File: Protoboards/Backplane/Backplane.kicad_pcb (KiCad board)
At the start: 2 copper layers, 129.5 x 142.2 mm, 2501 parts

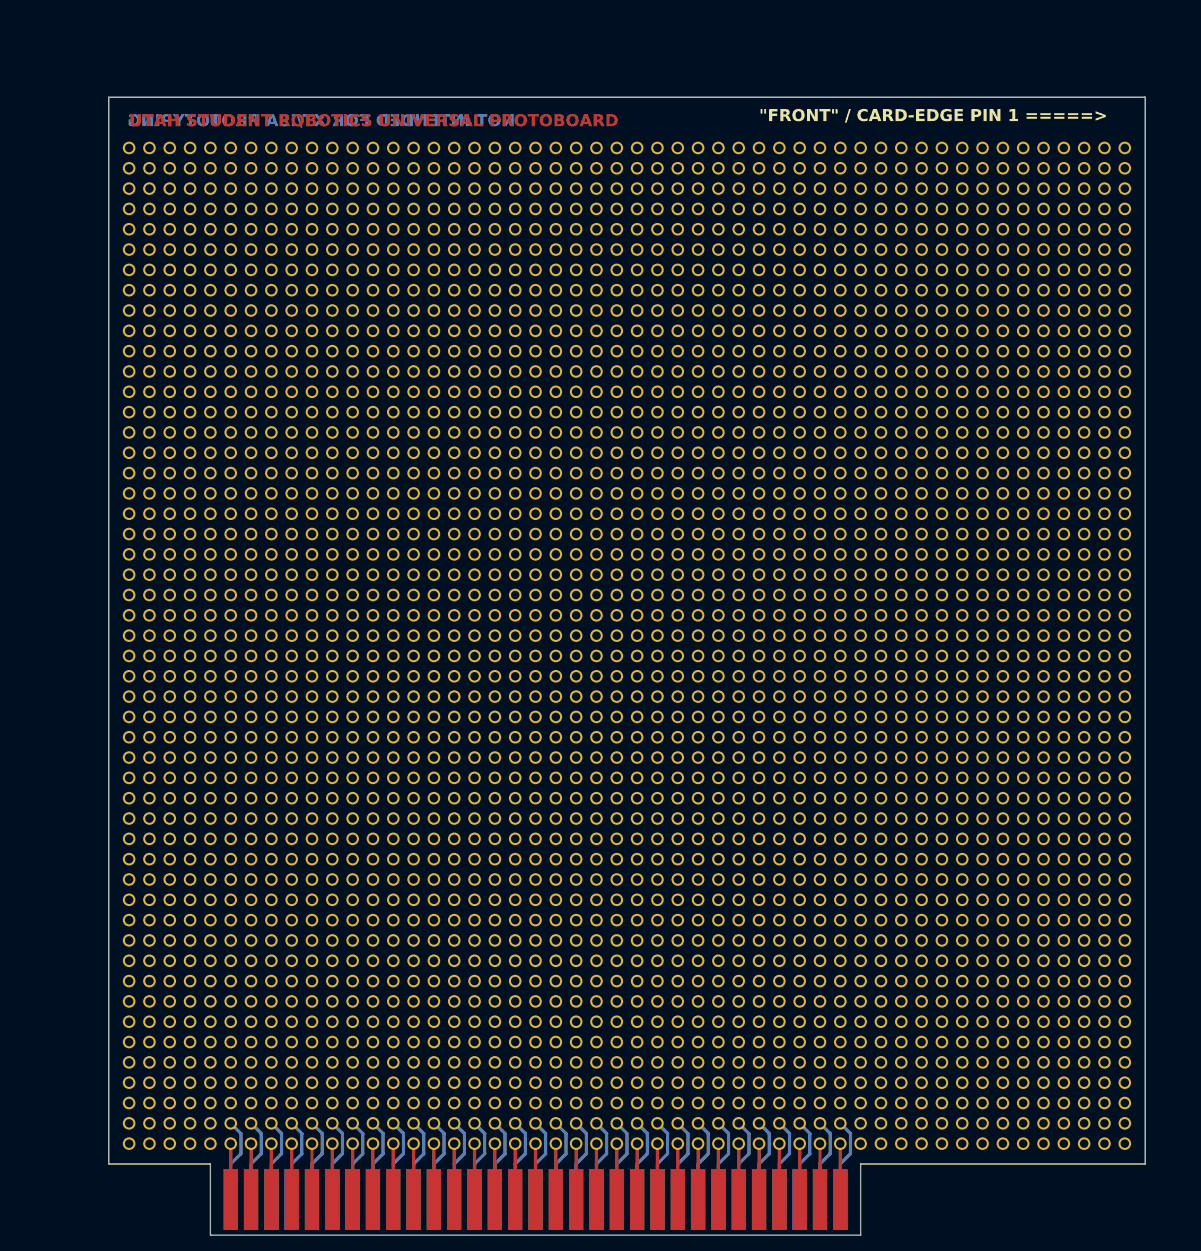
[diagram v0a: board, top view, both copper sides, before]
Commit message: Added dimensions to protoboard for reference as base backplane size
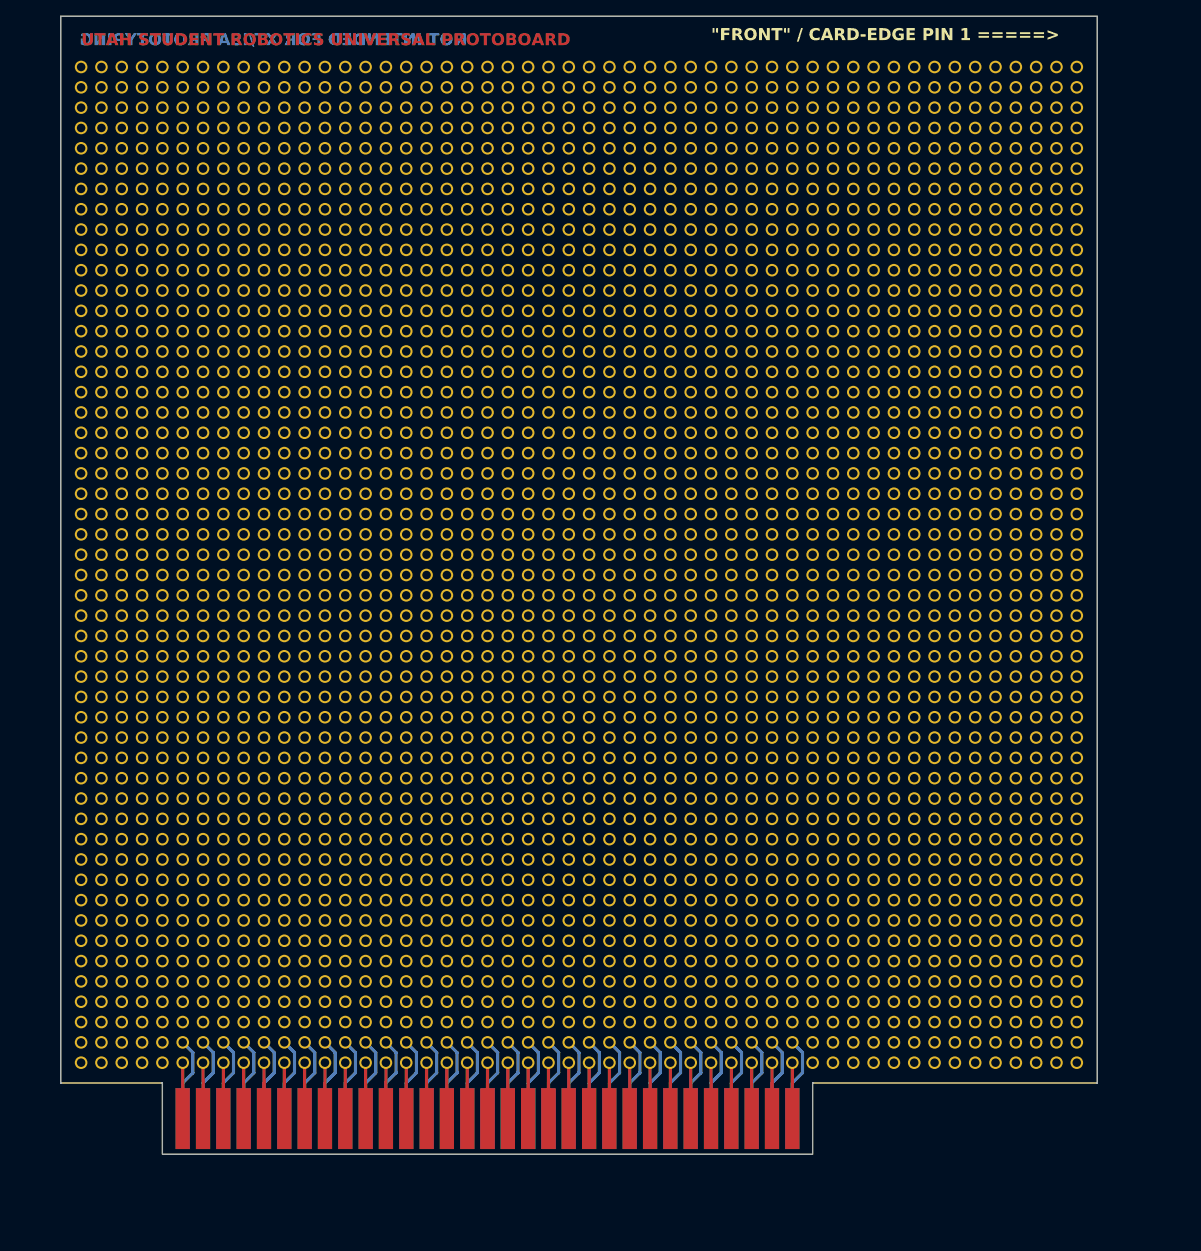
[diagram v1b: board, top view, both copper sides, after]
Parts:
- moved ? 11.8 mm to (126.1, 122.0)
- moved ? 11.8 mm to (60.0, 122.0)
- moved ? 11.8 mm to (128.6, 122.0)
- moved ? 11.8 mm to (113.4, 122.0)
- moved ? 11.8 mm to (103.2, 122.0)
- moved ? 11.8 mm to (42.3, 122.0)
- moved ? 11.8 mm to (108.3, 122.0)
- moved ? 11.8 mm to (62.6, 122.0)
- moved ? 11.8 mm to (121.0, 122.0)
- moved ? 11.8 mm to (55.0, 122.0)
- moved ? 11.8 mm to (19.4, 122.0)
- moved ? 11.8 mm to (75.3, 122.0)
- moved ? 11.8 mm to (136.2, 122.0)
- moved ? 11.8 mm to (65.1, 122.0)
- moved ? 11.8 mm to (141.3, 122.0)
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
